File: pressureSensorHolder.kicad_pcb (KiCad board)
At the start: 2 copper layers, 19 x 31 mm, 6 parts, among them J1 Conn_01x04, U1 SDP8xx-ANALOG

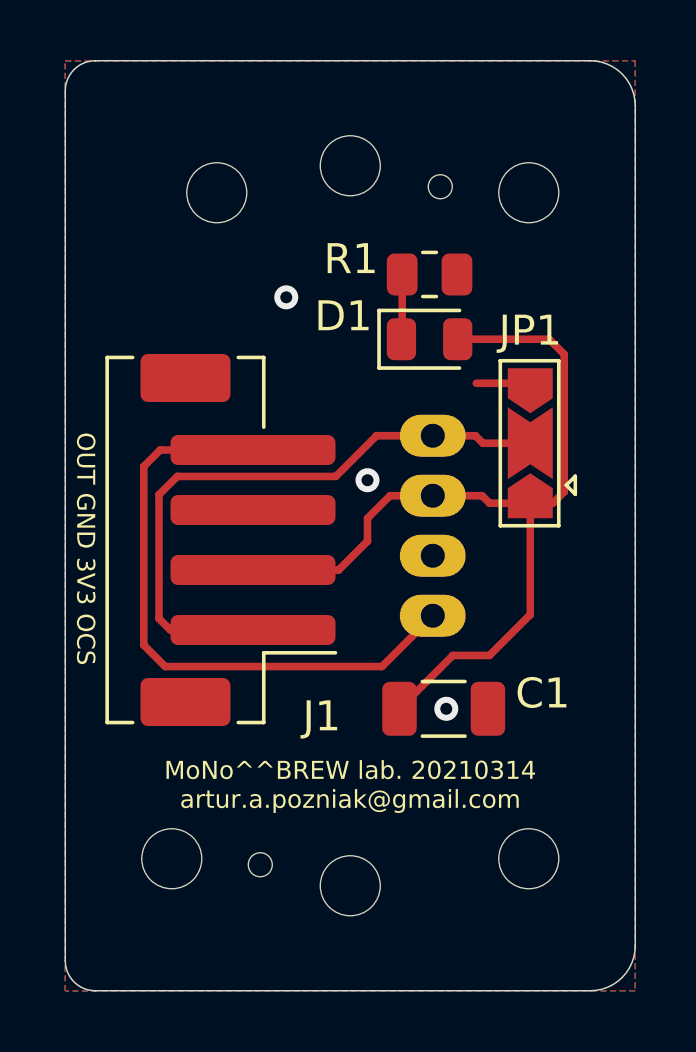
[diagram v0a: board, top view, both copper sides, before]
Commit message: New socket (JST/PH-1x03) and polishing. Production files (PCBWAY)
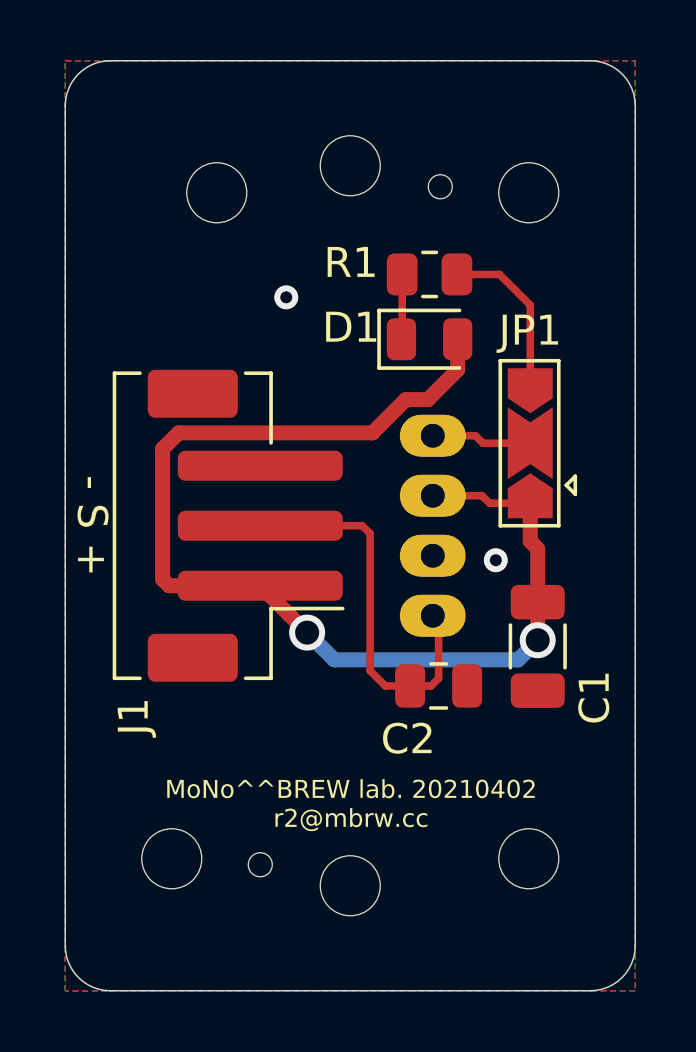
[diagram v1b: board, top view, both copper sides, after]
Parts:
- added C2: C, Capacitor_SMD:C_0805_2012Metric, F.Cu at (151.9, 89.0)
- J1: value Conn_01x04 -> Conn_01x03; footprint Connector_JST:JST_PH_B4B-PH-SM4-TB_1x04-1MP_P2.00mm_Vertical -> Connector_JST:JST_PH_B3B-PH-SM4-TB_1x03-1MP_P2.00mm_Vertical
- moved C1 3.76 mm to (155.2, 87.7), turned to 270 degrees
- moved J1 0.53 mm to (145.4, 83.7)
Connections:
- J1 pad 1: /OCS_SCL -> +3V3
- J1 pad 2: +3V3 -> /AOut_SDA
- JP1 pad : (no net) -> +3V3
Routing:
- net /OCS_SCL: track 20.7 -> 3.35 mm
- net +3V3: track 29.8 -> 38.2 mm, vias 0 -> 2
- net /AOut_SDA: track 20.5 -> 13.1 mm
- net GND: track 1.80 -> 5.47 mm, vias 3 -> 2
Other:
- outline, holes or cut-outs redrawn
- rule pad_to_mask_clearance: 0.051 -> 0
- board text added: "- S +"
- board text added: "MoNo^^BREW lab. 20210402 r2@mbrw.cc"
- board text removed: "MoNo^^BREW lab. 20210314 artur.a.pozniak@gmail.com"
- board text removed: "OUT GND 3V3 OCS"
